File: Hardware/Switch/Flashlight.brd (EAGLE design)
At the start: 38.1 x 50.8 mm, 27 parts

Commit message: Protos
This is what was sent out for protos.
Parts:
- added H3, H4: STAND-OFF, SparkFun-Hardware:STAND-OFF
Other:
- board text added: "Michelle Shorter"
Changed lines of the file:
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@@
 <layer number="49" name="Reference" color="7" fill="1" visible="yes" active="yes"/>
 <layer number="50" name="dxf" color="7" fill="1" visible="no" active="yes"/>
-<layer number="51" name="tDocu" color="6" fill="1" visible="no" active="yes"/>
+<layer number="51" name="tDocu" color="6" fill="1" visible="yes" active="yes"/>
 <layer number="52" name="bDocu" color="7" fill="1" visible="no" active="yes"/>
 <layer number="91" name="Nets" color="2" fill="1" visible="no" active="no"/>
@@
 <text x="18.161" y="40.005" size="2.54" layer="21" font="vector" rot="MR0">+</text>
 <rectangle x1="3.81" y1="16.383" x2="8.763" y2="38.989" layer="21"/>
+<text x="20.066" y="19.177" size="2.54" layer="21" font="vector" rot="MR0">+</text>
+<text x="19.812" y="4.318" size="2.54" layer="21" font="vector" rot="MR0">-</text>
+<dimension x1="34.29" y1="3.81" x2="38.1" y2="3.81" x3="36.195" y3="3.81" textsize="1.778" textratio="15" layer="49" dtype="horizontal" unit="inch"/>
+<dimension x1="3.81" y1="3.81" x2="0" y2="3.81" x3="1.905" y3="3.81" textsize="1.778" textratio="15" layer="49" dtype="horizontal" unit="inch"/>
+<text x="52.07" y="-8.89" size="1.778" layer="51" font="vector" ratio="15">Michelle Shorter</text>
 </plain>
 <attributes>
@@
 </class>
 </classes>
-<designrules name="default">
-<description language="en">&lt;b&gt;EAGLE Design Rules&lt;/b&gt;
-&lt;p&gt;
-The default Design Rules have been set to cover
-a wide range of applications. Your particular design
-may have different requirements, so please make the
-necessary adjustments and save your customized
-design rules under a new name.
-</description>
+<designrules name="SparkFun-2-layer-STANDARD">
+<description language="en">&lt;b&gt;SparkFun 2 Layer Design Rule Checks - STANDARD/TIGHT/FAB-LIMIT&lt;/b&gt;
+&lt;p&gt;
+These rules have been curated by SparkFuns DFM commitee. After doing much research, communicating with our multiple fab houses, and getting quotes of various designs, we have compiled three DRU files.
+&lt;p&gt;
+&lt;b&gt;STANDARD:&lt;/b&gt; This is more of a &quot;best case scenario&quot; set of limitations. If your design has the space, and/or you have the time to work within these parameters, please do. Larger trace width and clearance makes for easier visual inspection of the PCB while troubleshooting (useful in production and to the end user). It also allows for better ability to hack a trace (if you are crazy enough to scrape away the mask and solder to a trace). Another thing to keep in mind is that more metal is just more robust.
+&lt;p&gt;
+&lt;b&gt;TIGHT:&lt;/b&gt; This is where cost comes into play. We have found that most fab houses begin to add extra charges when you go smaller than these specs. In some cases, going to less than 15 mil trace can increase the cost by 10%. (This is why we have set the min drill on this DRU to 15 mil) Same story for traces thinner than 7 mil. To avoid those extra charges, then stay within the rules of this DRU.
+&lt;p&gt;
+&lt;b&gt;FAB-LIMIT:&lt;/b&gt; These set of rules are at the very limit of most fab houses capabilities. You will pay more for these specs, and it should be used on designs that have a darned good reason to need 4 mil vias and 4 mil traces.
+&lt;p&gt;
+**NOTE Clearance, Distance, Sizes, and Restring are all set to different limits in each of these three DRU files. Please compare the files within the CAM job editor window of eagle to see all the numbers.
+&lt;p&gt;
+***NOTE, Please set your Net Classes to default (0mil for all settings), so that it won't effect the DRC when you run it with these settings.</description>
 <param name="layerSetup" value="(1*16)"/>
 <param name="mtCopper" value="0.035mm 0.035mm 0.035mm 0.035mm 0.035mm 0.035mm 0.035mm 0.035mm 0.035mm 0.035mm 0.035mm 0.035mm 0.035mm 0.035mm 0.035mm 0.035mm"/>
 <param name="mtIsolate" value="1.5mm 0.15mm 0.2mm 0.15mm 0.2mm 0.15mm 0.2mm 0.15mm 0.2mm 0.15mm 0.2mm 0.15mm 0.2mm 0.15mm 0.2mm"/>
-<param name="mdWireWire" value="8mil"/>
+<param name="mdWireWire" value="10mil"/>
 <param name="mdWirePad" value="8mil"/>
-<param name="mdWireVia" value="8mil"/>
+<param name="mdWireVia" value="10mil"/>
 <param name="mdPadPad" value="8mil"/>
-<param name="mdPadVia" value="8mil"/>
-<param name="mdViaVia" value="8mil"/>
+<param name="mdPadVia" value="10mil"/>
+<param name="mdViaVia" value="10mil"/>
 <param name="mdSmdPad" value="8mil"/>
 <param name="mdSmdVia" value="8mil"/>
@@
 <param name="mdViaViaSameLayer" value="8mil"/>
 <param name="mnLayersViaInSmd" value="2"/>
-<param name="mdCopperDimension" value="40mil"/>
+<param name="mdCopperDimension" value="8mil"/>
 <param name="mdDrill" value="8mil"/>
 <param name="mdSmdStop" value="0mil"/>
 <param name="msWidth" value="10mil"/>
-<param name="msDrill" value="0.6mm"/>
+<param name="msDrill" value="20mil"/>
 <param name="msMicroVia" value="9.99mm"/>
 <param name="msBlindViaRatio" value="0.5"/>
@@
 <param name="rlMinPadBottom" value="10mil"/>
 <param name="rlMaxPadBottom" value="20mil"/>
-<param name="rlMinViaOuter" value="8mil"/>
+<param name="rlMinViaOuter" value="10mil"/>
 <param name="rlMaxViaOuter" value="20mil"/>
-<param name="rlMinViaInner" value="8mil"/>
+<param name="rlMinViaInner" value="10mil"/>
 <param name="rlMaxViaInner" value="20mil"/>
 <param name="rlMinMicroViaOuter" value="4mil"/>
@@
 <param name="mlMinCreamFrame" value="0mil"/>
 <param name="mlMaxCreamFrame" value="0mil"/>
-<param name="mlViaStopLimit" value="0mil"/>
+<param name="mlViaStopLimit" value="25mil"/>
 <param name="srRoundness" value="0"/>
 <param name="srMinRoundness" value="0mil"/>
@@
 <param name="dpMaxLengthDifference" value="10mm"/>
 <param name="dpGapFactor" value="2.5"/>
-<param name="checkAngle" value="0"/>
+<param name="checkAngle" value="1"/>
 <param name="checkFont" value="1"/>
 <param name="checkRestrict" value="1"/>
@@
 <param name="checkValues" value="0"/>
 <param name="useDiameter" value="13"/>
-<param name="maxErrors" value="999999"/>
+<param name="maxErrors" value="50"/>
 </designrules>
 <autorouter>
@@
 </autorouter>
 <elements>
-<element name="D1" library="SparkFun-LED" package="LED_5MM-KIT-NO-SILK" value="" x="19.05" y="39.37"/>
+<element name="D1" library="SparkFun-LED" package="LED_5MM-KIT-NO-SILK" value="" x="19.05" y="39.37">
+<attribute name="PROD_ID" value="9903" x="19.05" y="39.37" size="1.778" layer="27" display="off"/>
+</element>
 <element name="FRAME1" library="SparkFun-Aesthetics" package="CREATIVE_COMMONS" value="FRAME-LETTER" x="20.32" y="-8.89"/>
 <element name="LOGO1" library="SparkFun-Aesthetics" package="OSHW-LOGO-S" value="OSHW-LOGOS" x="3.048" y="10.414"/>
 <element name="R1" library="SparkFun-Resistors" package="AXIAL-0.3-KIT" value="330" x="12.7" y="30.48" rot="R90">
-<attribute name="PROD_ID" value=" " x="12.7" y="30.48" size="1.778" layer="27" rot="R90" display="off"/>
+<attribute name="PROD_ID" value="8371" x="12.7" y="30.48" size="1.778" layer="27" rot="R90" display="off"/>
 </element>
 <element name="LOGO2" library="SparkFun-Aesthetics" package="SFE_LOGO_FLAME_.1" value="SFE_LOGO_FLAME.1_INCH" x="34.29" y="8.89"/>
@@
 <element name="LOGO4" library="SparkFun-Aesthetics" package="SFE_LOGO_NAME_.1" value="SFE_LOGO_NAME.1_INCH" x="13.335" y="11.43"/>
 <element name="LOGO3" library="SparkFun-Aesthetics" package="SFE_LOGO_NAME_FLAME_.2" value="SFE_LOGO_NAME_FLAME.2_INCH" x="30.48" y="6.35" rot="MR0"/>
-<element name="BT2" library="SparkFun-Batteries" package="BATTCOM_20MM_PTH_KIT" value="" x="19.05" y="11.43" rot="R90"/>
+<element name="BT2" library="SparkFun-Batteries" package="BATTCOM_20MM_PTH_KIT" value="" x="19.05" y="11.43" rot="R90">
+<attribute name="PROD_ID" value="9031" x="19.05" y="11.43" size="1.778" layer="27" rot="R90" display="off"/>
+</element>
 <element name="U$2" library="buzzard_labels" package="BATTERY7" value="" x="22.352" y="25.4" rot="MR0"/>
 <element name="U$3" library="buzzard_labels" package="CR20328" value="" x="25.4" y="1.27"/>
@@
 <element name="U$10" library="flashlight#jpg" package="FLASHLIGHT#JPG" value="" x="19.05" y="30.48" rot="MR0"/>
 <element name="U$11" library="Label" package="THIS_FLASHLIGHT_BELONGS_TO#0" value="" x="2.54" y="15.24" rot="R90"/>
+<element name="H3" library="SparkFun-Hardware" package="STAND-OFF" value="STAND-OFF" x="3.81" y="43.18"/>
+<element name="H4" library="SparkFun-Hardware" package="STAND-OFF" value="STAND-OFF" x="34.29" y="43.18"/>
 </elements>
 <signals>

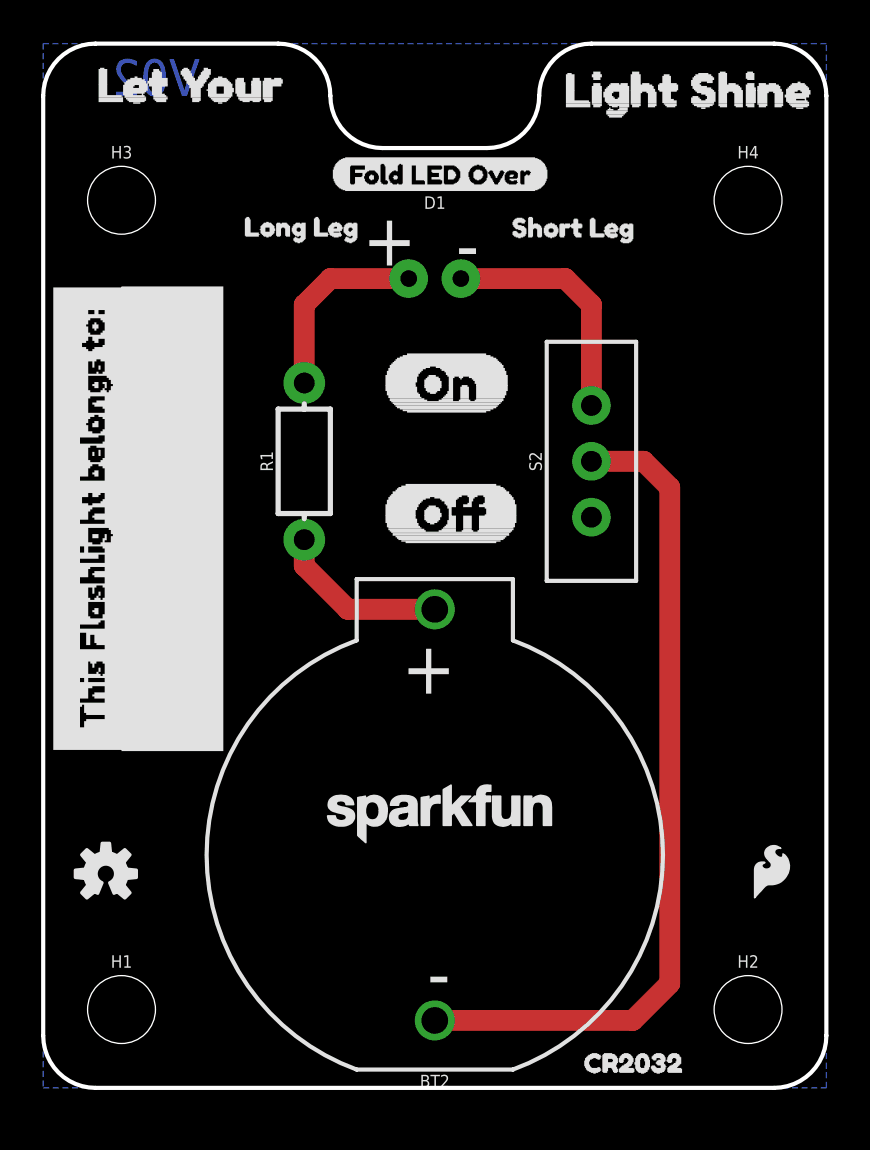
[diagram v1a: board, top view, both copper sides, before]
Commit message: Reds
Updated silk to be cleaner, updated version number
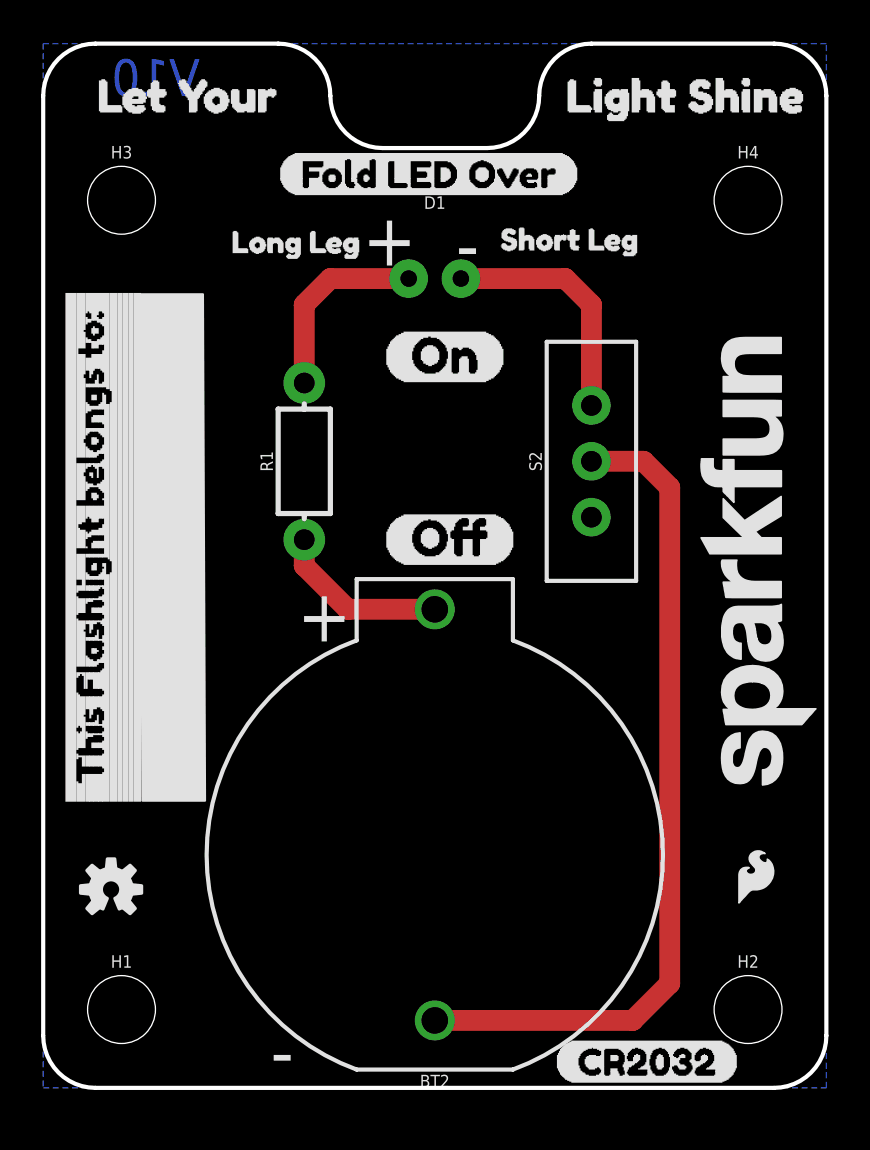
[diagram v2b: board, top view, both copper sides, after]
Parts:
- removed U$16: (no value), buzzard_labels:ON14
- LOGO4: value SFE_LOGO_NAME.1_INCH -> SFE_LOGO_NAME.2_INCH; device SparkFun-Aesthetics:SFE_LOGO_NAME_.1 -> SparkFun-Aesthetics:SFE_LOGO_NAME_.2
- R1: value 330 -> 10
- U$1: device buzzard_labels:OFF11 -> Flashlight_labels:CR20325
- U$10: device flashlight#jpg:FLASHLIGHT#JPG -> Flashlight_labels:SHORT_LEG1
- U$11: device Label:THIS_FLASHLIGHT_BELONGS_TO#0 -> Flashlight_labels:SPARKFUN#COM#FLASHLIGHT13
- U$12: device buzzard_labels:SWITCH6 -> Flashlight_labels:LED12
- U$13: device buzzard_labels:_SHORT_LEG3 -> Flashlight_labels:THIS_FLASHLIGHT_BELONGS_TO#10
- U$14: device buzzard_labels:LONG_LEG11 -> Flashlight_labels:RESISTOR14
- U$15: device buzzard_labels:SPARKFUN#COM#FLASHLIGHT13 -> Flashlight_labels:SWITCH13
- U$2: device buzzard_labels:BATTERY7 -> Flashlight_labels:FLASHLIGHT6
- U$3: device buzzard_labels:CR20328 -> Flashlight_labels:FOLD_LED_OVER0
- U$4: device buzzard_labels:FOLD_LED_OVER11 -> Flashlight_labels:BATTERY11
- U$5: device buzzard_labels:LED5 -> Flashlight_labels:LET_YOUR11
- U$6: device buzzard_labels:LET_YOUR0 -> Flashlight_labels:LIGHT_SHINE12
- U$7: device buzzard_labels:LIGHT_SHINE1 -> Flashlight_labels:LONG_LEG2
- U$8: device buzzard_labels:FLASHLIGHT12 -> Flashlight_labels:OFF4
- U$9: device buzzard_labels:RESISTOR4 -> Flashlight_labels:ON3
- moved U$3 45.4 mm to (11.4, 44.5)
- moved U$13 34.6 mm to (2.92, 12.8), turned to 90 degrees
- moved U$11 33.4 mm to (33.0, 1.52), flipped to the bottom, turned to 0 degrees
- moved U$1 28.0 mm to (24.9, 1.27)
- moved U$15 26.7 mm to (24.1, 26.7), turned to 90 degrees
- moved LOGO4 24.5 mm to (37.6, 14.7), turned to 90 degrees
- moved U$5 23.4 mm to (1.27, 48.3), flipped to the top
- moved U$6 23.1 mm to (24.1, 48.3)
- moved U$8 22.2 mm to (16.5, 26.7), flipped to the top
- moved U$4 21.6 mm to (24.1, 25.4), flipped to the bottom
- moved U$2 19.2 mm to (26.4, 6.60)
- moved U$7 17.2 mm to (8.26, 41.1)
- moved U$14 16.5 mm to (15.2, 26.7), flipped to the bottom, turned to 90 degrees
- moved U$10 11.0 mm to (21.3, 41.3), flipped to the top
- moved U$9 8.57 mm to (16.5, 35.6), flipped to the top, turned to 0 degrees
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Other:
- board text added: "V10"
- board text removed: "V02"
